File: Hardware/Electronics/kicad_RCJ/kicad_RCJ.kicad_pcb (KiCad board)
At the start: 2 copper layers, 113 x 151.1 mm, 78 parts, among them J10 Conn_01x04_M1_extra, J11 Conn_01x04_M2_extra, J12 Conn_01x04_M3_extra, J13 Conn_01x04_M4_extra, J14 Conn_01x06_teensy_left_extra, J15 Conn_01x04_teensy_right_extra, J16 Conn_01x07_IO_expander_extra, J17 Conn_02x03_I2C, J18 Conn_02x05_3V3_GND, J19 Conn_02x05_5V_GND, J2 Conn_01x06_IMU_extra, J20 Conn_01x06_BNO085_extra, J21 Conn_01x06_ISM20948_extra, J22 Conn_01x02_LSM5DSOX_LIS3MDL_e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, J23 VBAT_meas_conn, J24 Conn_01x02, J25 Conn_01x02, J26 Conn_01x02, J27 Conn_01x02, J28 Conn_01x02_5V, J29 Conn_01x02_3.3V, J3 Conn_01x02_colsens_interrupt, J4 Conn_01x02_5V, J5 Conn_01x02_3V3, J6 Conn_01x02_I2C1, J7 Conn_01x01_LOP, J8 Conn_01x03_IO_expander_interr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, J9 Conn_01x06_LED, M5 Servo1, M6 Servo2, U1 DRV8874, U12 VL53L0/1X, U13 VL53L0/1X, U14 VL53L0/1X, U15 VL53L0/1X, U16 VL53L0/1X, U17 VL53L0/1X, U18 VL53L0/1X, U2 DRV8874, U20 BNO085, U21 ICM20948, U22 LSM6DSOX+LIS3MDL, U23 TCS34725, U24 APDS9960, U25 VL53L0/1X, U3 DRV8874, U4 DRV8874

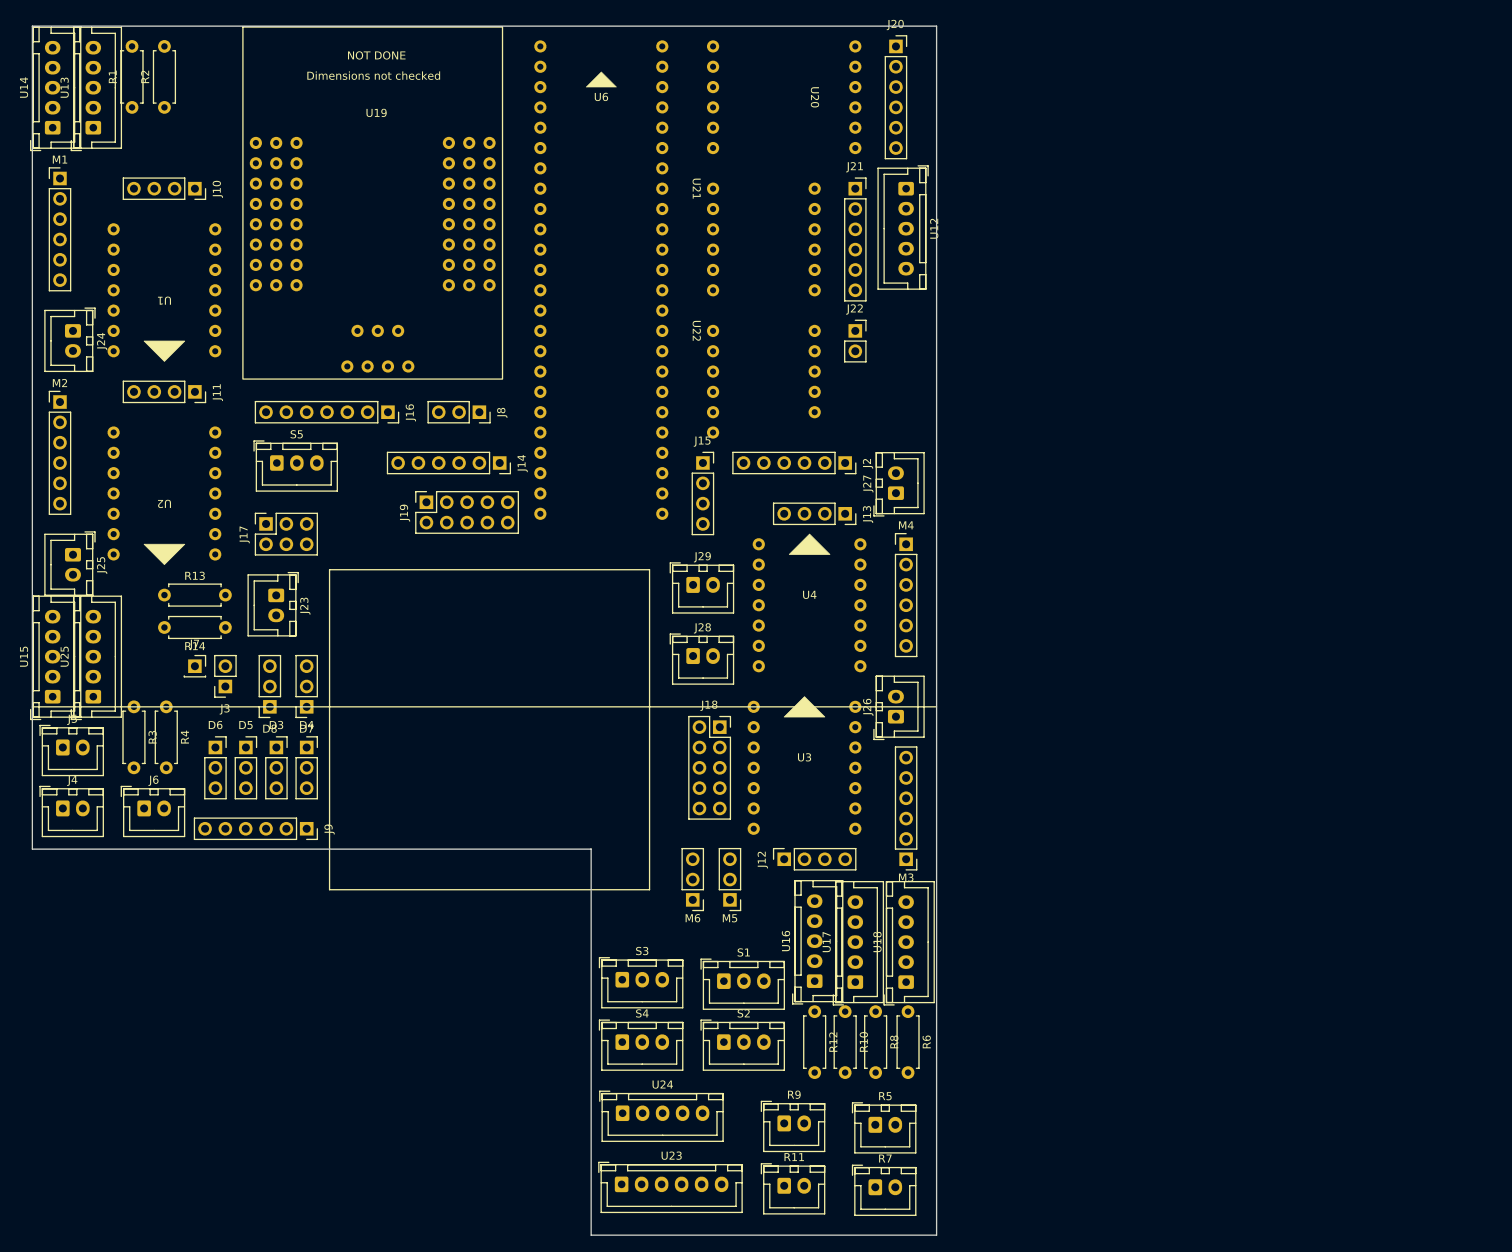
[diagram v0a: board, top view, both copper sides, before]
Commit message: updated PCB STEP for test in CAD
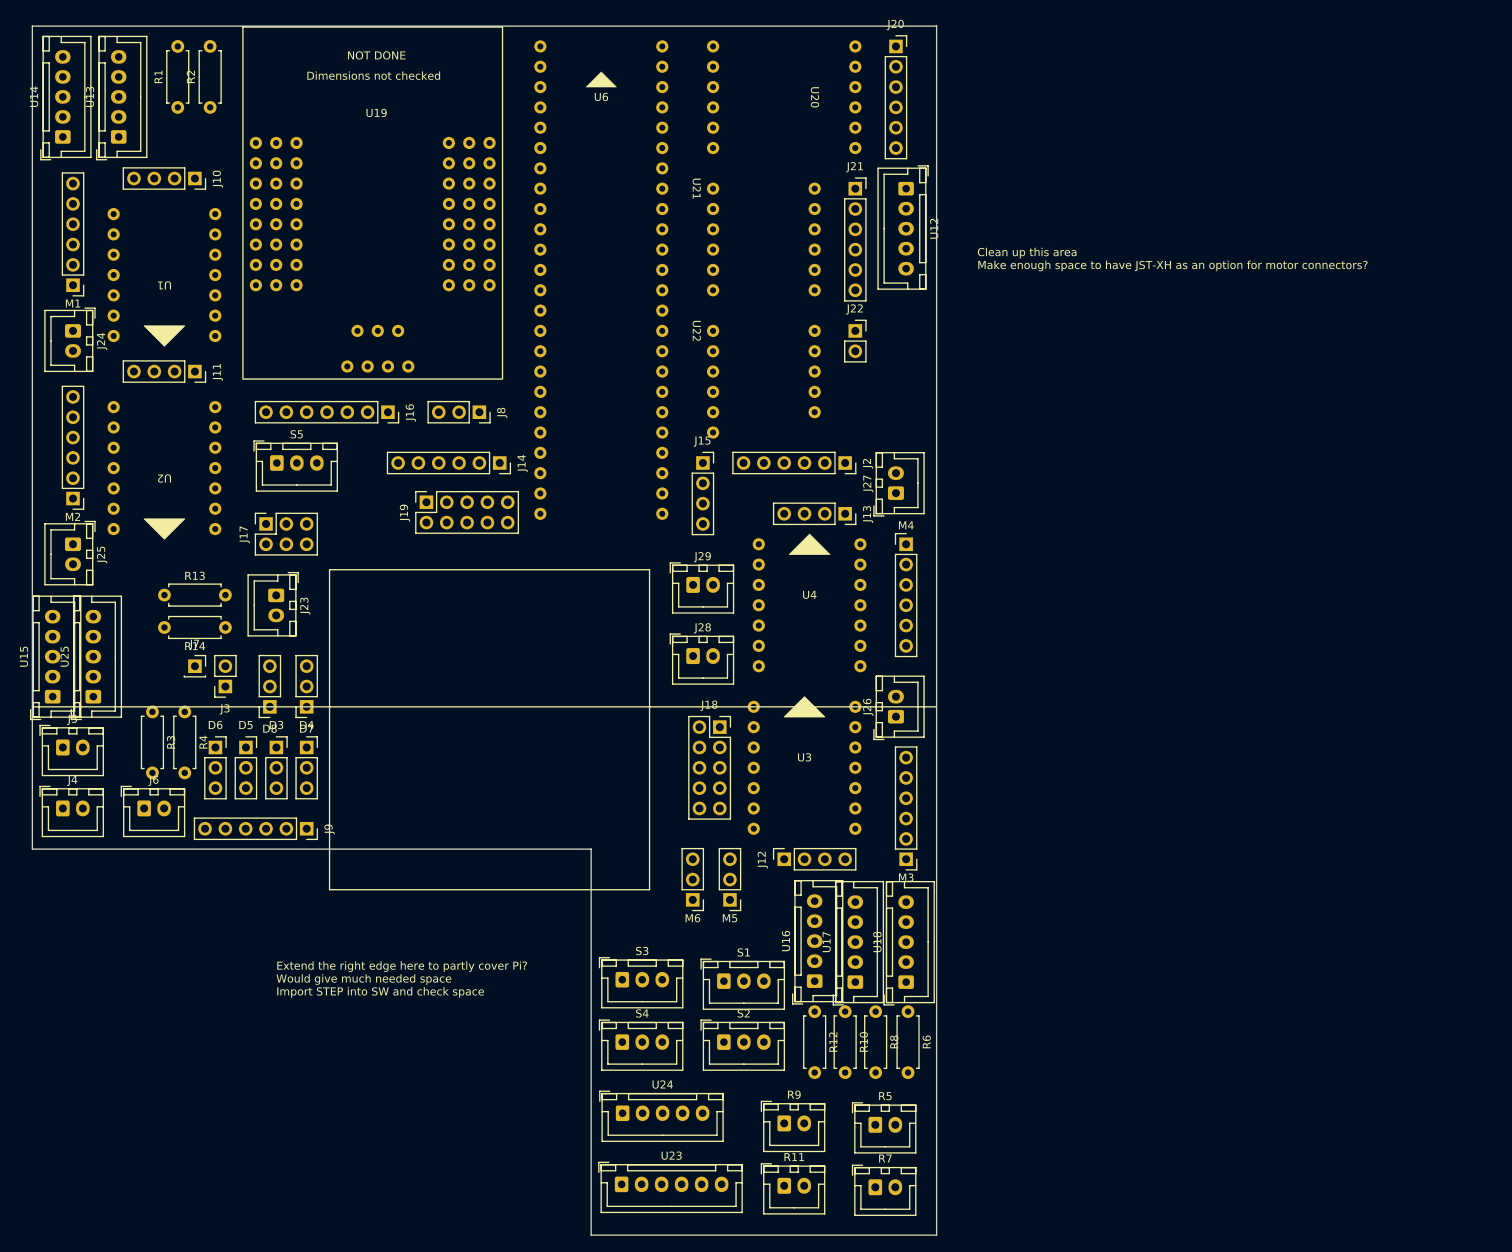
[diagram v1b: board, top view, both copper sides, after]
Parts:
- moved M1 13.4 mm to (38.1, 65.4), turned to 180 degrees
- moved M2 12.2 mm to (38.1, 92.1), turned to 180 degrees
- moved R1 5.72 mm to (51.2, 43.2)
- moved R2 5.71 mm to (55.2, 43.2)
- moved U13 3.38 mm to (43.8, 46.9)
- moved U2 3.17 mm to (55.9, 80.6)
- moved J11 2.54 mm to (53.3, 76.2)
- moved R3 2.40 mm to (48.0, 118.7)
- moved R4 2.40 mm to (52.1, 118.7)
- moved U1 1.91 mm to (55.9, 56.5)
- moved U14 1.71 mm to (36.8, 46.9)
- moved J25 1.31 mm to (38.1, 97.8)
- moved J10 1.27 mm to (53.3, 52.1)
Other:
- board text added: "Clean up this area Make enough space to have JST-XH as an option for motor connectors?"
- board text added: "Extend the right edge here to partly cover Pi? Would give much needed space Import STEP into SW and check space"
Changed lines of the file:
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@@
   )
   (footprint "Resistor_THT:R_Axial_DIN0207_L6.3mm_D2.5mm_P7.62mm_Horizontal" (layer "F.Cu")
-    (at 49.76 118.11 -90)
+    (at 52.07 118.745 -90)
     (descr "Resistor, Axial_DIN0207 series, Axial, Horizontal, pin pitch=7.62mm, 0.25W = 1/4W, length*diameter=6.3*2.5mm^2, http://cdn-reichelt.de/documents/datenblatt/B400/1_4W%23YAG.pdf")
     (tags "Resistor Axial_DIN0207 series Axial Horizontal pin pitch 7.62mm 0.25W = 1/4W length 6.3mm diameter 2.5mm")
@@
   )
   (footprint "Connector_PinHeader_2.54mm:PinHeader_1x06_P2.54mm_Vertical" (layer "F.Cu")
-    (at 36.4744 52.07)
+    (at 38.1 65.405 180)
     (descr "Through hole straight pin header, 1x06, 2.54mm pitch, single row")
     (tags "Through hole pin header THT 1x06 2.54mm single row")
@@
     (fp_line (start 1.27 13.97) (end -1.27 13.97)
       (stroke (width 0.1) (type solid)) (layer "F.Fab"))
-    (pad "1" thru_hole rect (at 0 0) (size 1.7 1.7) (drill 1) (layers "*.Cu" "*.Mask")
+    (pad "1" thru_hole rect (at 0 0 180) (size 1.7 1.7) (drill 1) (layers "*.Cu" "*.Mask")
       (net 73 "Net-(U1-OUT1)") (pinfunction "M_PWR") (pintype "power_in"))
-    (pad "2" thru_hole oval (at 0 2.54) (size 1.7 1.7) (drill 1) (layers "*.Cu" "*.Mask")
+    (pad "2" thru_hole oval (at 0 2.54 180) (size 1.7 1.7) (drill 1) (layers "*.Cu" "*.Mask")
       (net 74 "Net-(U1-OUT2)") (pinfunction "M_PWR") (pintype "power_in"))
-    (pad "3" thru_hole oval (at 0 5.08) (size 1.7 1.7) (drill 1) (layers "*.Cu" "*.Mask")
+    (pad "3" thru_hole oval (at 0 5.08 180) (size 1.7 1.7) (drill 1) (layers "*.Cu" "*.Mask")
       (net 1 "GND") (pinfunction "GND_ENC") (pintype "power_in"))
-    (pad "4" thru_hole oval (at 0 7.62) (size 1.7 1.7) (drill 1) (layers "*.Cu" "*.Mask")
+    (pad "4" thru_hole oval (at 0 7.62 180) (size 1.7 1.7) (drill 1) (layers "*.Cu" "*.Mask")
       (net 17 "+3.3V") (pinfunction "VCC_ENC") (pintype "power_in"))
-    (pad "5" thru_hole oval (at 0 10.16) (size 1.7 1.7) (drill 1) (layers "*.Cu" "*.Mask")
+    (pad "5" thru_hole oval (at 0 10.16 180) (size 1.7 1.7) (drill 1) (layers "*.Cu" "*.Mask")
       (net 75 "Net-(M1-ENC_A_OUT)") (pinfunction "ENC_A_OUT") (pintype "output"))
-    (pad "6" thru_hole oval (at 0 12.7) (size 1.7 1.7) (drill 1) (layers "*.Cu" "*.Mask")
+    (pad "6" thru_hole oval (at 0 12.7 180) (size 1.7 1.7) (drill 1) (layers "*.Cu" "*.Mask")
       (net 76 "Net-(M1-ENC_B_OUTPUT)") (pinfunction "ENC_B_OUTPUT") (pintype "output"))
     (model "${KICAD6_3DMODEL_DIR}/Connector_PinHeader_2.54mm.3dshapes/PinHeader_1x06_P2.54mm_Vertical.wrl"
@@
   )
   (footprint "Connector_PinHeader_2.54mm:PinHeader_1x06_P2.54mm_Vertical" (layer "F.Cu")
-    (at 36.4744 80.01)
+    (at 38.1 92.075 180)
     (descr "Through hole straight pin header, 1x06, 2.54mm pitch, single row")
     (tags "Through hole pin header THT 1x06 2.54mm single row")
@@
     (fp_line (start 1.27 13.97) (end -1.27 13.97)
       (stroke (width 0.1) (type solid)) (layer "F.Fab"))
-    (pad "1" thru_hole rect (at 0 0) (size 1.7 1.7) (drill 1) (layers "*.Cu" "*.Mask")
+    (pad "1" thru_hole rect (at 0 0 180) (size 1.7 1.7) (drill 1) (layers "*.Cu" "*.Mask")
       (net 77 "Net-(U2-OUT1)") (pinfunction "M_PWR") (pintype "power_in"))
-    (pad "2" thru_hole oval (at 0 2.54) (size 1.7 1.7) (drill 1) (layers "*.Cu" "*.Mask")
+    (pad "2" thru_hole oval (at 0 2.54 180) (size 1.7 1.7) (drill 1) (layers "*.Cu" "*.Mask")
       (net 78 "Net-(U2-OUT2)") (pinfunction "M_PWR") (pintype "power_in"))
-    (pad "3" thru_hole oval (at 0 5.08) (size 1.7 1.7) (drill 1) (layers "*.Cu" "*.Mask")
+    (pad "3" thru_hole oval (at 0 5.08 180) (size 1.7 1.7) (drill 1) (layers "*.Cu" "*.Mask")
       (net 1 "GND") (pinfunction "GND_ENC") (pintype "power_in"))
-    (pad "4" thru_hole oval (at 0 7.62) (size 1.7 1.7) (drill 1) (layers "*.Cu" "*.Mask")
+    (pad "4" thru_hole oval (at 0 7.62 180) (size 1.7 1.7) (drill 1) (layers "*.Cu" "*.Mask")
       (net 17 "+3.3V") (pinfunction "VCC_ENC") (pintype "power_in"))
-    (pad "5" thru_hole oval (at 0 10.16) (size 1.7 1.7) (drill 1) (layers "*.Cu" "*.Mask")
+    (pad "5" thru_hole oval (at 0 10.16 180) (size 1.7 1.7) (drill 1) (layers "*.Cu" "*.Mask")
       (net 79 "Net-(M2-ENC_A_OUT)") (pinfunction "ENC_A_OUT") (pintype "output"))
-    (pad "6" thru_hole oval (at 0 12.7) (size 1.7 1.7) (drill 1) (layers "*.Cu" "*.Mask")
+    (pad "6" thru_hole oval (at 0 12.7 180) (size 1.7 1.7) (drill 1) (layers "*.Cu" "*.Mask")
       (net 80 "Net-(M2-ENC_B_OUTPUT)") (pinfunction "ENC_B_OUTPUT") (pintype "output"))
     (model "${KICAD6_3DMODEL_DIR}/Connector_PinHeader_2.54mm.3dshapes/PinHeader_1x06_P2.54mm_Vertical.wrl"
@@
   )
   (footprint "Resistor_THT:R_Axial_DIN0207_L6.3mm_D2.5mm_P7.62mm_Horizontal" (layer "F.Cu")
-    (at 49.53 43.18 90)
+    (at 55.245 43.18 90)
     (descr "Resistor, Axial_DIN0207 series, Axial, Horizontal, pin pitch=7.62mm, 0.25W = 1/4W, length*diameter=6.3*2.5mm^2, http://cdn-reichelt.de/documents/datenblatt/B400/1_4W%23YAG.pdf")
     (tags "Resistor Axial_DIN0207 series Axial Horizontal pin pitch 7.62mm 0.25W = 1/4W length 6.3mm diameter 2.5mm")
@@
   )
   (footprint "Connector_JST:JST_XH_B5B-XH-A_1x05_P2.50mm_Vertical" (layer "F.Cu")
-    (at 35.56 45.72 90)
+    (at 36.83 46.87 90)
     (descr "JST XH series connector, B5B-XH-A (http://www.jst-mfg.com/product/pdf/eng/eXH.pdf), generated with kicad-footprint-generator")
     (tags "connector JST XH vertical")
@@
   )
   (footprint "Connector_PinSocket_2.54mm:PinSocket_1x04_P2.54mm_Vertical" (layer "F.Cu")
-    (at 53.34 78.74 -90)
+    (at 53.34 76.2 -90)
     (descr "Through hole straight socket strip, 1x04, 2.54mm pitch, single row (from Kicad 4.0.7), script generated")
     (tags "Through hole socket strip THT 1x04 2.54mm single row")
@@
   )
   (footprint "Connector_PinSocket_2.54mm:PinSocket_1x04_P2.54mm_Vertical" (layer "F.Cu")
-    (at 53.34 53.34 -90)
+    (at 53.34 52.07 -90)
     (descr "Through hole straight socket strip, 1x04, 2.54mm pitch, single row (from Kicad 4.0.7), script generated")
     (tags "Through hole socket strip THT 1x04 2.54mm single row")
@@
   )
   (footprint "Connector_JST:JST_XH_B2B-XH-A_1x02_P2.50mm_Vertical" (layer "F.Cu")
-    (at 38.1 99.1 -90)
+    (at 38.1 97.79 -90)
     (descr "JST XH series connector, B2B-XH-A (http://www.jst-mfg.com/product/pdf/eng/eXH.pdf), generated with kicad-footprint-generator")
     (tags "connector JST XH vertical")
@@
   )
   (footprint "Resistor_THT:R_Axial_DIN0207_L6.3mm_D2.5mm_P7.62mm_Horizontal" (layer "F.Cu")
-    (at 45.72 118.11 -90)
+    (at 48.03 118.745 -90)
     (descr "Resistor, Axial_DIN0207 series, Axial, Horizontal, pin pitch=7.62mm, 0.25W = 1/4W, length*diameter=6.3*2.5mm^2, http://cdn-reichelt.de/documents/datenblatt/B400/1_4W%23YAG.pdf")
     (tags "Resistor Axial_DIN0207 series Axial Horizontal pin pitch 7.62mm 0.25W = 1/4W length 6.3mm diameter 2.5mm")
@@
   )
   (footprint "RCJ2024_kicad_footprints:DRV8874" (layer "F.Cu")
-    (at 55.88 83.82 180)
+    (at 55.88 80.645 180)
     (property "Sheetfile" "kicad_RCJ.kicad_sch")
     (property "Sheetname" "")
@@
   )
   (footprint "Connector_JST:JST_XH_B5B-XH-A_1x05_P2.50mm_Vertical" (layer "F.Cu")
-    (at 40.64 45.72 90)
+    (at 43.815 46.87 90)
     (descr "JST XH series connector, B5B-XH-A (http://www.jst-mfg.com/product/pdf/eng/eXH.pdf), generated with kicad-footprint-generator")
     (tags "connector JST XH vertical")
@@
   )
   (footprint "RCJ2024_kicad_footprints:DRV8874" (layer "F.Cu")
-    (at 55.88 58.42 180)
+    (at 55.88 56.515 180)
     (property "Sheetfile" "kicad_RCJ.kicad_sch")
     (property "Sheetname" "")
@@
   )
   (footprint "Resistor_THT:R_Axial_DIN0207_L6.3mm_D2.5mm_P7.62mm_Horizontal" (layer "F.Cu")
-    (at 45.48 43.18 90)
+    (at 51.195 43.18 90)
     (descr "Resistor, Axial_DIN0207 series, Axial, Horizontal, pin pitch=7.62mm, 0.25W = 1/4W, length*diameter=6.3*2.5mm^2, http://cdn-reichelt.de/documents/datenblatt/B400/1_4W%23YAG.pdf")
     (tags "Resistor Axial_DIN0207 series Axial Horizontal pin pitch 7.62mm 0.25W = 1/4W length 6.3mm diameter 2.5mm")
@@
   (gr_line (start 102.87 184.15) (end 146.05 184.15)
     (stroke (width 0.15) (type default)) (layer "Edge.Cuts"))
+  (gr_text "Extend the right edge here to partly cover Pi?\nWould give much needed space\nImport STEP into SW and check space" (at 63.5 154.305) (layer "F.SilkS")
+    (effects (font (size 1 1) (thickness 0.15)) (justify left bottom))
+  )
+  (gr_text "Clean up this area\nMake enough space to have JST-XH as an option for motor connectors?" (at 151.13 63.5) (layer "F.SilkS")
+    (effects (font (size 1 1) (thickness 0.15)) (justify left bottom))
+  )
 )
